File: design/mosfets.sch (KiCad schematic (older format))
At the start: 15 parts, among them Q1 IRFS3006, Q2 IRFS3006, Q3 IRFS3006, Q4 IRFS3006, Q5 IRFS3006, Q6 IRFS3006

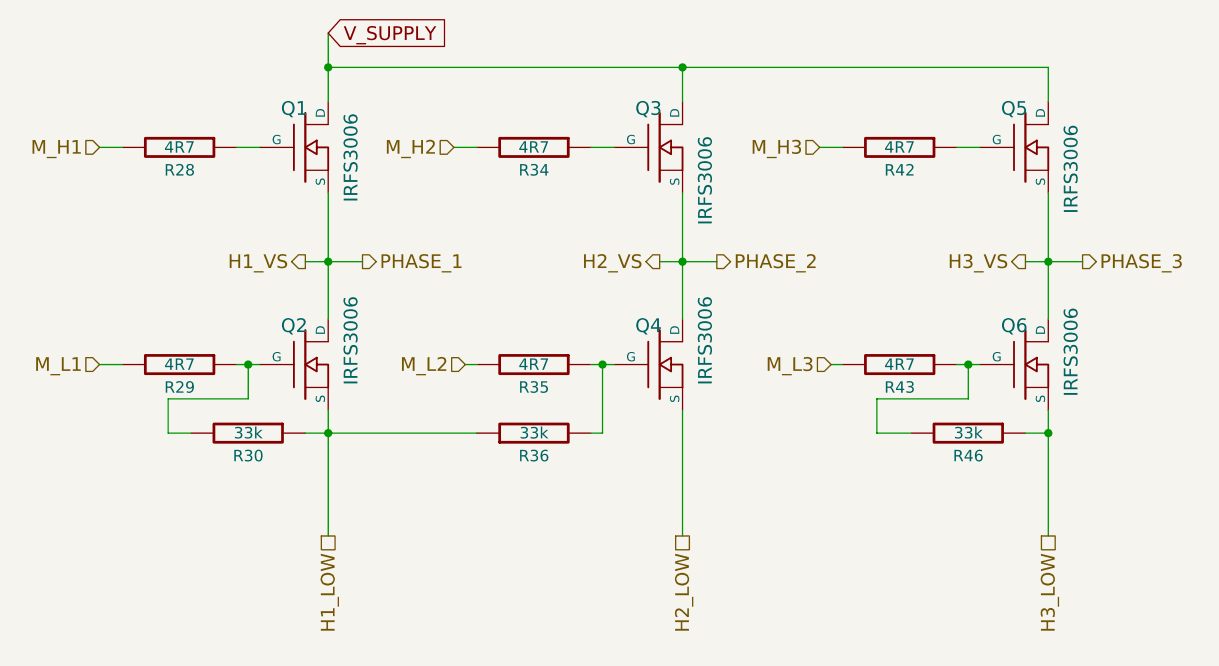
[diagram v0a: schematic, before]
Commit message: Add a electronic for second motor and add new pin's for it on MCU; TODO Add new mosfets
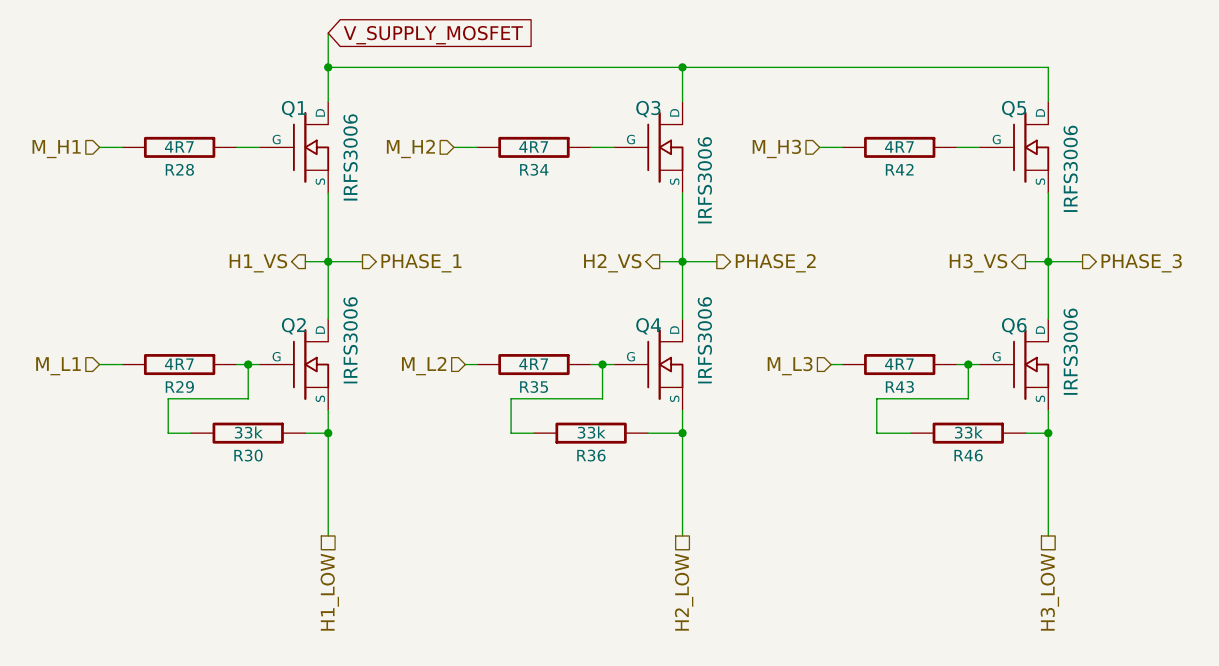
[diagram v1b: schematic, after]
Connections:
- net H1_LOW: no longer R36.1
- net H2_LOW: now also R36.2
- net at Q4.G, R35.1: now also R36.1; no longer R36.2
- net V_SUPPLY renamed V_SUPPLY_MOSFET
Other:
- moved on the sheet: R36
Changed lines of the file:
@@
 $Descr A4 11693 8268
 encoding utf-8
-Sheet 2 8
+Sheet 2 11
 Title "BLDC Driver 4.6"
-Date "10 jan 2015"
+Date "13 jan 2015"
 Rev "4.6"
 Comp "Benjamin Vedder"
@@
 U 1 1 53F8E60B
 P 7850 4050
+AR Path="/53F826DC/53F8E60B" Ref="R46"  Part="1"
+AR Path="/54B73596/53F8E60B" Ref="R46"  Part="1"
 F 0 "R46" V 7950 4050 50  0000 C CNN
 F 1 "33k" V 7850 4050 50  0000 C CNN
@@
 U 1 1 53F8E612
 P 4700 4050
+AR Path="/53F826DC/53F8E612" Ref="R30"  Part="1"
+AR Path="/54B73596/53F8E612" Ref="R30"  Part="1"
 F 0 "R30" V 4800 4050 50  0000 C CNN
 F 1 "33k" V 4700 4050 50  0000 C CNN
@@
 U 1 1 53F8E63D
 P 4950 2800
+AR Path="/53F826DC/53F8E63D" Ref="Q1"  Part="1"
+AR Path="/54B73596/53F8E63D" Ref="Q1"  Part="1"
 F 0 "Q1" H 4960 2970 60  0000 R CNN
 F 1 "IRFS3006" V 5150 2950 60  0000 R CNN
@@
 U 1 1 53F8E644
 P 4950 3750
+AR Path="/53F826DC/53F8E644" Ref="Q2"  Part="1"
+AR Path="/54B73596/53F8E644" Ref="Q2"  Part="1"
 F 0 "Q2" H 4960 3920 60  0000 R CNN
 F 1 "IRFS3006" V 5150 4050 60  0000 R CNN
@@
 U 1 1 53F8E64B
 P 4400 3750
+AR Path="/53F826DC/53F8E64B" Ref="R29"  Part="1"
+AR Path="/54B73596/53F8E64B" Ref="R29"  Part="1"
 F 0 "R29" V 4500 3750 50  0000 C CNN
 F 1 "4R7" V 4400 3750 50  0000 C CNN
@@
 U 1 1 53F8E652
 P 4400 2800
+AR Path="/53F826DC/53F8E652" Ref="R28"  Part="1"
+AR Path="/54B73596/53F8E652" Ref="R28"  Part="1"
 F 0 "R28" V 4500 2800 50  0000 C CNN
 F 1 "4R7" V 4400 2800 50  0000 C CNN
@@
 U 1 1 53F8E65E
 P 5950 2800
+AR Path="/53F826DC/53F8E65E" Ref="R34"  Part="1"
+AR Path="/54B73596/53F8E65E" Ref="R34"  Part="1"
 F 0 "R34" V 6050 2800 50  0000 C CNN
 F 1 "4R7" V 5950 2800 50  0000 C CNN
@@
 U 1 1 53F8E665
 P 5950 3750
+AR Path="/53F826DC/53F8E665" Ref="R35"  Part="1"
+AR Path="/54B73596/53F8E665" Ref="R35"  Part="1"
 F 0 "R35" V 6050 3750 50  0000 C CNN
 F 1 "4R7" V 5950 3750 50  0000 C CNN
@@
 U 1 1 53F8E66C
 P 6500 3750
+AR Path="/53F826DC/53F8E66C" Ref="Q4"  Part="1"
+AR Path="/54B73596/53F8E66C" Ref="Q4"  Part="1"
 F 0 "Q4" H 6510 3920 60  0000 R CNN
 F 1 "IRFS3006" V 6700 4050 60  0000 R CNN
@@
 U 1 1 53F8E673
 P 6500 2800
+AR Path="/53F826DC/53F8E673" Ref="Q3"  Part="1"
+AR Path="/54B73596/53F8E673" Ref="Q3"  Part="1"
 F 0 "Q3" H 6510 2970 60  0000 R CNN
 F 1 "IRFS3006" V 6700 2850 60  0000 R CNN
@@
 U 1 1 53F8E67A
 P 8100 2800
+AR Path="/53F826DC/53F8E67A" Ref="Q5"  Part="1"
+AR Path="/54B73596/53F8E67A" Ref="Q5"  Part="1"
 F 0 "Q5" H 8110 2970 60  0000 R CNN
 F 1 "IRFS3006" V 8300 2900 60  0000 R CNN
@@
 U 1 1 53F8E681
 P 8100 3750
+AR Path="/53F826DC/53F8E681" Ref="Q6"  Part="1"
+AR Path="/54B73596/53F8E681" Ref="Q6"  Part="1"
 F 0 "Q6" H 8110 3920 60  0000 R CNN
 F 1 "IRFS3006" V 8300 4000 60  0000 R CNN
@@
 U 1 1 53F8E688
 P 7550 3750
+AR Path="/53F826DC/53F8E688" Ref="R43"  Part="1"
+AR Path="/54B73596/53F8E688" Ref="R43"  Part="1"
 F 0 "R43" V 7650 3750 50  0000 C CNN
 F 1 "4R7" V 7550 3750 50  0000 C CNN
@@
 U 1 1 53F8E68F
 P 7550 2800
+AR Path="/53F826DC/53F8E68F" Ref="R42"  Part="1"
+AR Path="/54B73596/53F8E68F" Ref="R42"  Part="1"
 F 0 "R42" V 7650 2800 50  0000 C CNN
 F 1 "4R7" V 7550 2800 50  0000 C CNN
@@
 L R R36
 U 1 1 53F8E69C
-P 5950 4050
-F 0 "R36" V 5850 4050 50  0000 C CNN
-F 1 "33k" V 5950 4050 50  0000 C CNN
-F 2 "SMD_Packages:SMD-0603_r" H 5950 4050 60  0001 C CNN
-F 3 "" H 5950 4050 60  0001 C CNN
-	1    5950 4050
+P 6200 4050
+AR Path="/53F826DC/53F8E69C" Ref="R36"  Part="1"
+AR Path="/54B73596/53F8E69C" Ref="R36"  Part="1"
+F 0 "R36" V 6100 4050 50  0000 C CNN
+F 1 "33k" V 6200 4050 50  0000 C CNN
+F 2 "SMD_Packages:SMD-0603_r" H 6200 4050 60  0001 C CNN
+F 3 "" H 6200 4050 60  0001 C CNN
+	1    6200 4050
 	0    -1   -1   0
 $EndComp
@@
 	8100 4050 8200 4050
 Wire Wire Line
-	4950 4050 5700 4050
+	4950 4050 5050 4050
 Wire Wire Line
 	7250 3750 7300 3750
@@
 Connection ~ 5050 4050
 Connection ~ 6250 3750
-Wire Wire Line
-	6200 4050 6250 4050
-Wire Wire Line
-	6250 4050 6250 3750
 Text GLabel 5050 2300 2    60   Input ~ 0
-V_SUPPLY
+V_SUPPLY_MOSFET
 Wire Wire Line
 	6600 3950 6600 4500
@@
 00 00 00 41 83 58 05 00 00 08 1A C4 2A 00 00 40 D0 20 56 01 00 00 82 06 B1 0A 00 00 10 34 88 55
 00 00 80 A0 41 AC 02 00 00 04 CD FF 03 15 B2 0E 9E 1D 9F E2 F2 00 00 00 00 49 45 4E 44 AE 42 60
-82 C8 $EndBitmap
+82 59 $EndBitmap
 EndData
 $EndBitmap
@@
 Wire Wire Line
 	4350 4050 4450 4050
+Wire Wire Line
+	6250 3750 6250 3900
+Wire Wire Line
+	6250 3900 5850 3900
+Wire Wire Line
+	5850 3900 5850 4050
+Wire Wire Line
+	5850 4050 5950 4050
+Wire Wire Line
+	6450 4050 6600 4050
+Connection ~ 6600 4050
 $EndSCHEMATC

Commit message: Make change in annotations and some small fixes
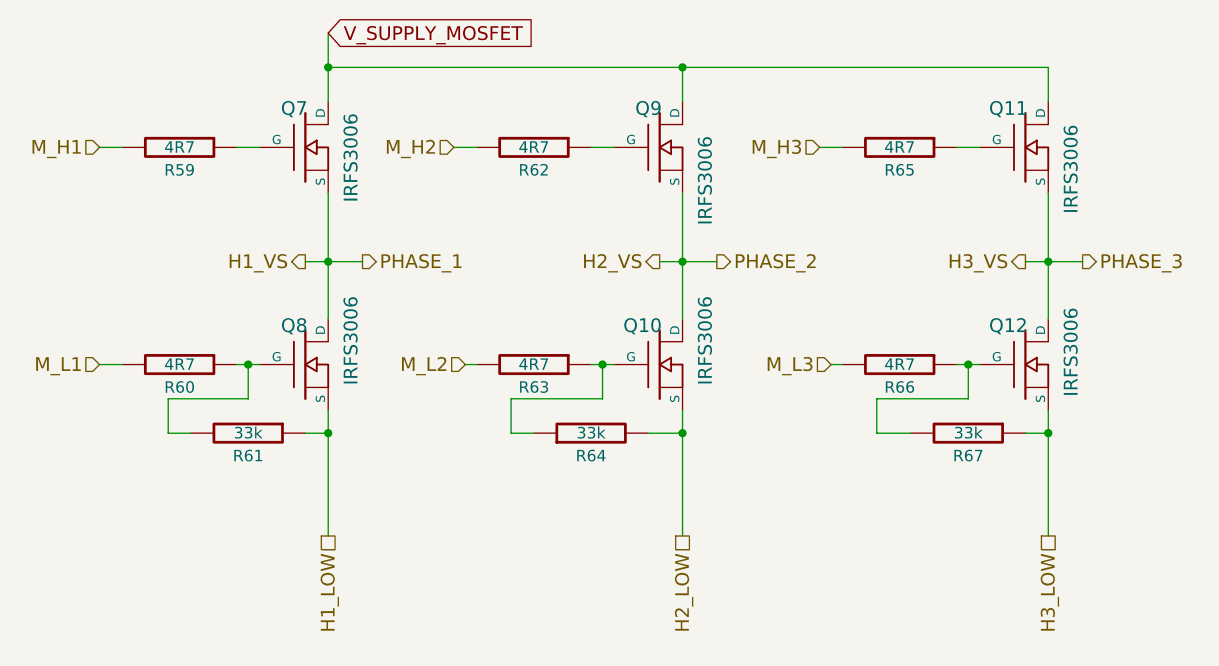
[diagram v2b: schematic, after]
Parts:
- renumbered Q4 to Q10, Q5 to Q11, Q6 to Q12, Q1 to Q7, Q2 to Q8, Q3 to Q9, R28 to R59, R29 to R60, R30 to R61, R34 to R62, R35 to R63, R36 to R64, R42 to R65, R43 to R66, R46 to R67
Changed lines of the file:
@@
 $Descr A4 11693 8268
 encoding utf-8
-Sheet 2 11
+Sheet 8 10
 Title "BLDC Driver 4.6"
-Date "13 jan 2015"
+Date "16 jan 2015"
 Rev "4.6"
 Comp "Benjamin Vedder"
@@
 $EndDescr
 $Comp
-L R R46
+L R R67
 U 1 1 53F8E60B
 P 7850 4050
-AR Path="/53F826DC/53F8E60B" Ref="R46"  Part="1"
-AR Path="/54B73596/53F8E60B" Ref="R46"  Part="1"
-F 0 "R46" V 7950 4050 50  0000 C CNN
+AR Path="/54B73596/53F8E60B" Ref="R67"  Part="1"
+AR Path="/53F826DC/53F8E60B" Ref="R22"  Part="1"
+F 0 "R67" V 7950 4050 50  0000 C CNN
 F 1 "33k" V 7850 4050 50  0000 C CNN
 F 2 "SMD_Packages:SMD-0603_r" H 7850 4050 60  0001 C CNN
@@
 $EndComp
 $Comp
-L R R30
+L R R61
 U 1 1 53F8E612
 P 4700 4050
-AR Path="/53F826DC/53F8E612" Ref="R30"  Part="1"
-AR Path="/54B73596/53F8E612" Ref="R30"  Part="1"
-F 0 "R30" V 4800 4050 50  0000 C CNN
+AR Path="/54B73596/53F8E612" Ref="R61"  Part="1"
+AR Path="/53F826DC/53F8E612" Ref="R16"  Part="1"
+F 0 "R61" V 4800 4050 50  0000 C CNN
 F 1 "33k" V 4700 4050 50  0000 C CNN
 F 2 "SMD_Packages:SMD-0603_r" H 4700 4050 60  0001 C CNN
@@
 $EndComp
 $Comp
-L MOSFET_N Q1
+L MOSFET_N Q7
 U 1 1 53F8E63D
 P 4950 2800
+AR Path="/54B73596/53F8E63D" Ref="Q7"  Part="1"
 AR Path="/53F826DC/53F8E63D" Ref="Q1"  Part="1"
-AR Path="/54B73596/53F8E63D" Ref="Q1"  Part="1"
-F 0 "Q1" H 4960 2970 60  0000 R CNN
+F 0 "Q7" H 4960 2970 60  0000 R CNN
 F 1 "IRFS3006" V 5150 2950 60  0000 R CNN
 F 2 "CRF1:D2PAK-7-GDS" H 4950 2800 60  0001 C CNN
@@
 $EndComp
 $Comp
-L MOSFET_N Q2
+L MOSFET_N Q8
 U 1 1 53F8E644
 P 4950 3750
+AR Path="/54B73596/53F8E644" Ref="Q8"  Part="1"
 AR Path="/53F826DC/53F8E644" Ref="Q2"  Part="1"
-AR Path="/54B73596/53F8E644" Ref="Q2"  Part="1"
-F 0 "Q2" H 4960 3920 60  0000 R CNN
+F 0 "Q8" H 4960 3920 60  0000 R CNN
 F 1 "IRFS3006" V 5150 4050 60  0000 R CNN
 F 2 "CRF1:D2PAK-7-GDS" H 4950 3750 60  0001 C CNN
@@
 $EndComp
 $Comp
-L R R29
+L R R60
 U 1 1 53F8E64B
 P 4400 3750
-AR Path="/53F826DC/53F8E64B" Ref="R29"  Part="1"
-AR Path="/54B73596/53F8E64B" Ref="R29"  Part="1"
-F 0 "R29" V 4500 3750 50  0000 C CNN
+AR Path="/54B73596/53F8E64B" Ref="R60"  Part="1"
+AR Path="/53F826DC/53F8E64B" Ref="R15"  Part="1"
+F 0 "R60" V 4500 3750 50  0000 C CNN
 F 1 "4R7" V 4400 3750 50  0000 C CNN
 F 2 "SMD_Packages:SMD-0603_r" H 4400 3750 60  0001 C CNN
@@
 $EndComp
 $Comp
-L R R28
+L R R59
 U 1 1 53F8E652
 P 4400 2800
-AR Path="/53F826DC/53F8E652" Ref="R28"  Part="1"
-AR Path="/54B73596/53F8E652" Ref="R28"  Part="1"
-F 0 "R28" V 4500 2800 50  0000 C CNN
+AR Path="/54B73596/53F8E652" Ref="R59"  Part="1"
+AR Path="/53F826DC/53F8E652" Ref="R14"  Part="1"
+F 0 "R59" V 4500 2800 50  0000 C CNN
 F 1 "4R7" V 4400 2800 50  0000 C CNN
 F 2 "SMD_Packages:SMD-0603_r" H 4400 2800 60  0001 C CNN
@@
 $EndComp
 $Comp
-L R R34
+L R R62
 U 1 1 53F8E65E
 P 5950 2800
-AR Path="/53F826DC/53F8E65E" Ref="R34"  Part="1"
-AR Path="/54B73596/53F8E65E" Ref="R34"  Part="1"
-F 0 "R34" V 6050 2800 50  0000 C CNN
+AR Path="/54B73596/53F8E65E" Ref="R62"  Part="1"
+AR Path="/53F826DC/53F8E65E" Ref="R17"  Part="1"
+F 0 "R62" V 6050 2800 50  0000 C CNN
 F 1 "4R7" V 5950 2800 50  0000 C CNN
 F 2 "SMD_Packages:SMD-0603_r" H 5950 2800 60  0001 C CNN
@@
 $EndComp
 $Comp
-L R R35
+L R R63
 U 1 1 53F8E665
 P 5950 3750
-AR Path="/53F826DC/53F8E665" Ref="R35"  Part="1"
-AR Path="/54B73596/53F8E665" Ref="R35"  Part="1"
-F 0 "R35" V 6050 3750 50  0000 C CNN
+AR Path="/54B73596/53F8E665" Ref="R63"  Part="1"
+AR Path="/53F826DC/53F8E665" Ref="R18"  Part="1"
+F 0 "R63" V 6050 3750 50  0000 C CNN
 F 1 "4R7" V 5950 3750 50  0000 C CNN
 F 2 "SMD_Packages:SMD-0603_r" H 5950 3750 60  0001 C CNN
@@
 $EndComp
 $Comp
-L MOSFET_N Q4
+L MOSFET_N Q10
 U 1 1 53F8E66C
 P 6500 3750
+AR Path="/54B73596/53F8E66C" Ref="Q10"  Part="1"
 AR Path="/53F826DC/53F8E66C" Ref="Q4"  Part="1"
-AR Path="/54B73596/53F8E66C" Ref="Q4"  Part="1"
-F 0 "Q4" H 6510 3920 60  0000 R CNN
+F 0 "Q10" H 6510 3920 60  0000 R CNN
 F 1 "IRFS3006" V 6700 4050 60  0000 R CNN
 F 2 "CRF1:D2PAK-7-GDS" H 6500 3750 60  0001 C CNN
@@
 $EndComp
 $Comp
-L MOSFET_N Q3
+L MOSFET_N Q9
 U 1 1 53F8E673
 P 6500 2800
+AR Path="/54B73596/53F8E673" Ref="Q9"  Part="1"
 AR Path="/53F826DC/53F8E673" Ref="Q3"  Part="1"
-AR Path="/54B73596/53F8E673" Ref="Q3"  Part="1"
-F 0 "Q3" H 6510 2970 60  0000 R CNN
+F 0 "Q9" H 6510 2970 60  0000 R CNN
 F 1 "IRFS3006" V 6700 2850 60  0000 R CNN
 F 2 "CRF1:D2PAK-7-GDS" H 6500 2800 60  0001 C CNN
@@
 $EndComp
 $Comp
-L MOSFET_N Q5
+L MOSFET_N Q11
 U 1 1 53F8E67A
 P 8100 2800
+AR Path="/54B73596/53F8E67A" Ref="Q11"  Part="1"
 AR Path="/53F826DC/53F8E67A" Ref="Q5"  Part="1"
-AR Path="/54B73596/53F8E67A" Ref="Q5"  Part="1"
-F 0 "Q5" H 8110 2970 60  0000 R CNN
+F 0 "Q11" H 8110 2970 60  0000 R CNN
 F 1 "IRFS3006" V 8300 2900 60  0000 R CNN
 F 2 "CRF1:D2PAK-7-GDS" H 8100 2800 60  0001 C CNN
@@
 $EndComp
 $Comp
-L MOSFET_N Q6
+L MOSFET_N Q12
 U 1 1 53F8E681
 P 8100 3750
+AR Path="/54B73596/53F8E681" Ref="Q12"  Part="1"
 AR Path="/53F826DC/53F8E681" Ref="Q6"  Part="1"
-AR Path="/54B73596/53F8E681" Ref="Q6"  Part="1"
-F 0 "Q6" H 8110 3920 60  0000 R CNN
+F 0 "Q12" H 8110 3920 60  0000 R CNN
 F 1 "IRFS3006" V 8300 4000 60  0000 R CNN
 F 2 "CRF1:D2PAK-7-GDS" H 8100 3750 60  0001 C CNN
@@
 $EndComp
 $Comp
-L R R43
+L R R66
 U 1 1 53F8E688
 P 7550 3750
-AR Path="/53F826DC/53F8E688" Ref="R43"  Part="1"
-AR Path="/54B73596/53F8E688" Ref="R43"  Part="1"
-F 0 "R43" V 7650 3750 50  0000 C CNN
+AR Path="/54B73596/53F8E688" Ref="R66"  Part="1"
+AR Path="/53F826DC/53F8E688" Ref="R21"  Part="1"
+F 0 "R66" V 7650 3750 50  0000 C CNN
 F 1 "4R7" V 7550 3750 50  0000 C CNN
 F 2 "SMD_Packages:SMD-0603_r" H 7550 3750 60  0001 C CNN
@@
 $EndComp
 $Comp
-L R R42
+L R R65
 U 1 1 53F8E68F
 P 7550 2800
-AR Path="/53F826DC/53F8E68F" Ref="R42"  Part="1"
-AR Path="/54B73596/53F8E68F" Ref="R42"  Part="1"
-F 0 "R42" V 7650 2800 50  0000 C CNN
+AR Path="/54B73596/53F8E68F" Ref="R65"  Part="1"
+AR Path="/53F826DC/53F8E68F" Ref="R20"  Part="1"
+F 0 "R65" V 7650 2800 50  0000 C CNN
 F 1 "4R7" V 7550 2800 50  0000 C CNN
 F 2 "SMD_Packages:SMD-0603_r" H 7550 2800 60  0001 C CNN
@@
 $EndComp
 $Comp
-L R R36
+L R R64
 U 1 1 53F8E69C
 P 6200 4050
-AR Path="/53F826DC/53F8E69C" Ref="R36"  Part="1"
-AR Path="/54B73596/53F8E69C" Ref="R36"  Part="1"
-F 0 "R36" V 6100 4050 50  0000 C CNN
+AR Path="/54B73596/53F8E69C" Ref="R64"  Part="1"
+AR Path="/53F826DC/53F8E69C" Ref="R19"  Part="1"
+F 0 "R64" V 6100 4050 50  0000 C CNN
 F 1 "33k" V 6200 4050 50  0000 C CNN
 F 2 "SMD_Packages:SMD-0603_r" H 6200 4050 60  0001 C CNN
@@
 00 00 00 41 83 58 05 00 00 08 1A C4 2A 00 00 40 D0 20 56 01 00 00 82 06 B1 0A 00 00 10 34 88 55
 00 00 80 A0 41 AC 02 00 00 04 CD FF 03 15 B2 0E 9E 1D 9F E2 F2 00 00 00 00 49 45 4E 44 AE 42 60
-82 59 $EndBitmap
+82 9F $EndBitmap
 EndData
 $EndBitmap
